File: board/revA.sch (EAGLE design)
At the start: 37 parts, among them IC1 74HCT125D, Q1 VND7NV04, Q2 VND7NV04, Q3 VND7NV04, Q4 VND7NV04

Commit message: Changing buffer package to TSSOP
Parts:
- IC1: value 74HCT125D -> 74HCT125; device 74xx-eu:74HCT125D -> 74xx-eu:74ABT125PW
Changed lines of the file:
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@@
 <grid distance="0.05" unitdist="inch" unit="inch" style="lines" multiple="1" display="yes" altdistance="0.005" altunitdist="inch" altunit="inch"/>
 <layers>
-<layer number="1" name="Top" color="4" fill="1" visible="no" active="no"/>
-<layer number="16" name="Bottom" color="1" fill="1" visible="no" active="no"/>
-<layer number="17" name="Pads" color="2" fill="1" visible="no" active="no"/>
-<layer number="18" name="Vias" color="2" fill="1" visible="no" active="no"/>
-<layer number="19" name="Unrouted" color="6" fill="1" visible="no" active="no"/>
-<layer number="20" name="Dimension" color="24" fill="1" visible="no" active="no"/>
-<layer number="21" name="tPlace" color="7" fill="1" visible="no" active="no"/>
-<layer number="22" name="bPlace" color="7" fill="1" visible="no" active="no"/>
-<layer number="23" name="tOrigins" color="15" fill="1" visible="no" active="no"/>
-<layer number="24" name="bOrigins" color="15" fill="1" visible="no" active="no"/>
-<layer number="25" name="tNames" color="7" fill="1" visible="no" active="no"/>
-<layer number="26" name="bNames" color="7" fill="1" visible="no" active="no"/>
-<layer number="27" name="tValues" color="7" fill="1" visible="no" active="no"/>
-<layer number="28" name="bValues" color="7" fill="1" visible="no" active="no"/>
+<layer number="1" name="Top" color="4" fill="1" visible="yes" active="no"/>
+<layer number="16" name="Bottom" color="1" fill="1" visible="yes" active="no"/>
+<layer number="17" name="Pads" color="2" fill="1" visible="yes" active="no"/>
+<layer number="18" name="Vias" color="2" fill="1" visible="yes" active="no"/>
+<layer number="19" name="Unrouted" color="6" fill="1" visible="yes" active="no"/>
+<layer number="20" name="Dimension" color="24" fill="1" visible="yes" active="no"/>
+<layer number="21" name="tPlace" color="7" fill="1" visible="yes" active="no"/>
+<layer number="22" name="bPlace" color="7" fill="1" visible="yes" active="no"/>
+<layer number="23" name="tOrigins" color="15" fill="1" visible="yes" active="no"/>
+<layer number="24" name="bOrigins" color="15" fill="1" visible="yes" active="no"/>
+<layer number="25" name="tNames" color="7" fill="1" visible="yes" active="no"/>
+<layer number="26" name="bNames" color="7" fill="1" visible="yes" active="no"/>
+<layer number="27" name="tValues" color="7" fill="1" visible="yes" active="no"/>
+<layer number="28" name="bValues" color="7" fill="1" visible="yes" active="no"/>
 <layer number="29" name="tStop" color="7" fill="3" visible="no" active="no"/>
 <layer number="30" name="bStop" color="7" fill="6" visible="no" active="no"/>
@@
 <layer number="35" name="tGlue" color="7" fill="4" visible="no" active="no"/>
 <layer number="36" name="bGlue" color="7" fill="5" visible="no" active="no"/>
-<layer number="37" name="tTest" color="7" fill="1" visible="no" active="no"/>
-<layer number="38" name="bTest" color="7" fill="1" visible="no" active="no"/>
+<layer number="37" name="tTest" color="7" fill="1" visible="yes" active="no"/>
+<layer number="38" name="bTest" color="7" fill="1" visible="yes" active="no"/>
 <layer number="39" name="tKeepout" color="4" fill="11" visible="no" active="no"/>
 <layer number="40" name="bKeepout" color="1" fill="11" visible="no" active="no"/>
@@
 <layer number="44" name="Drills" color="7" fill="1" visible="no" active="no"/>
 <layer number="45" name="Holes" color="7" fill="1" visible="no" active="no"/>
-<layer number="46" name="Milling" color="3" fill="1" visible="no" active="no"/>
-<layer number="47" name="Measures" color="7" fill="1" visible="no" active="no"/>
-<layer number="48" name="Document" color="7" fill="1" visible="no" active="no"/>
-<layer number="49" name="Reference" color="7" fill="1" visible="no" active="no"/>
-<layer number="50" name="dxf" color="7" fill="1" visible="no" active="no"/>
-<layer number="51" name="tDocu" color="7" fill="1" visible="no" active="no"/>
-<layer number="52" name="bDocu" color="7" fill="1" visible="no" active="no"/>
-<layer number="53" name="tGND_GNDA" color="7" fill="9" visible="no" active="no"/>
-<layer number="54" name="bGND_GNDA" color="1" fill="9" visible="no" active="no"/>
-<layer number="56" name="wert" color="7" fill="1" visible="no" active="no"/>
-<layer number="57" name="tCAD" color="7" fill="1" visible="no" active="no"/>
-<layer number="59" name="tCarbon" color="7" fill="1" visible="no" active="no"/>
-<layer number="60" name="bCarbon" color="7" fill="1" visible="no" active="no"/>
+<layer number="46" name="Milling" color="3" fill="1" visible="yes" active="no"/>
+<layer number="47" name="Measures" color="7" fill="1" visible="yes" active="no"/>
+<layer number="48" name="Document" color="7" fill="1" visible="yes" active="no"/>
+<layer number="49" name="Reference" color="7" fill="1" visible="yes" active="no"/>
+<layer number="50" name="dxf" color="7" fill="1" visible="yes" active="no"/>
+<layer number="51" name="tDocu" color="7" fill="1" visible="yes" active="no"/>
+<layer number="52" name="bDocu" color="7" fill="1" visible="yes" active="no"/>
+<layer number="53" name="tGND_GNDA" color="7" fill="9" visible="yes" active="no"/>
+<layer number="54" name="bGND_GNDA" color="1" fill="9" visible="yes" active="no"/>
+<layer number="56" name="wert" color="7" fill="1" visible="yes" active="no"/>
+<layer number="57" name="tCAD" color="7" fill="1" visible="yes" active="no"/>
+<layer number="59" name="tCarbon" color="7" fill="1" visible="yes" active="no"/>
+<layer number="60" name="bCarbon" color="7" fill="1" visible="yes" active="no"/>
 <layer number="88" name="SimResults" color="9" fill="1" visible="yes" active="yes"/>
 <layer number="89" name="SimProbes" color="9" fill="1" visible="yes" active="yes"/>
@@
 <part name="UART" library="SparkFun-Connectors" library_urn="urn:adsk.eagle:library:513" deviceset="CONN_03" device="" package3d_urn="urn:adsk.eagle:package:38063/1"/>
 <part name="GND13" library="supply1" library_urn="urn:adsk.eagle:library:371" deviceset="GND" device=""/>
-<part name="IC1" library="74xx-eu" library_urn="urn:adsk.eagle:library:85" deviceset="74*125" device="D" package3d_urn="urn:adsk.eagle:package:1010/2" technology="HCT"/>
+<part name="IC1" library="74xx-eu" library_urn="urn:adsk.eagle:library:85" deviceset="74*125" device="PW" package3d_urn="urn:adsk.eagle:package:2019/1" technology="ABT" value="74HCT125"/>
 <part name="P+2" library="supply1" library_urn="urn:adsk.eagle:library:371" deviceset="+5V" device=""/>
 <part name="GND14" library="supply1" library_urn="urn:adsk.eagle:library:371" deviceset="GND" device=""/>

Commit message: Adding wires, protections, switch
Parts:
- added D10, D11, D8, D9: BAT54S, diode:BAT54S
- added K1: (no value), Seeed-Switch:SMD-SWITCH-TACTILE-SPST-NO(4P-D6.0MM)
- added R12, R13, R14, R15, R16: 10k, rcl:R-EU_R0603
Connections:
- removed net INJ1_FAKE: INJ.1, R7.1
- removed net INJ2_FAKE: INJ.2, R8.1
- removed net INJ3_FAKE: INJ.3, R9.1
- removed net INJ4_FAKE: INJ.4, R10.1
- new net BUTTON1: MCUPORTC.PC13
- new net INJ1_FREQ: D8.C1A2, MCUPORTA_L.PA6, R12.1
- new net INJ1_IN: INJ.1, R12.2, R7.1
- new net INJ2_FREQ: D9.C1A2, MCUPORTA_L.PA7, R13.1
- new net INJ2_IN: INJ.2, R13.2, R8.1
- new net INJ3_FREQ: D10.C1A2, MCUPORTB_L.PB0, R14.1
- new net INJ3_IN: INJ.3, R14.2, R9.1
- new net INJ4_FREQ: D11.C1A2, MCUPORTB_L.PB1, R15.1
- new net INJ4_IN: INJ.4, R10.1, R15.2
- new net N$3: K1.A0, K1.A1, MCURESET.BOOT0, R16.1
- new net SPI_MISO: MCUPORTB_H.PB14
- new net SPI_MOSI: MCUPORTB_H.PB15
- new net SPI_NSS: MCUPORTB_H.PB12
- new net SPI_SCK: MCUPORTB_H.PB13
- net +3V3: now also D10.C2, D11.C2, D8.C2, D9.C2, K1.B0, K1.B1; no longer MCURESET.BOOT0
- net AN_0: now also MCUPORTA_L.PA0
- net AN_1: now also MCUPORTA_L.PA4
- net GND: now also D10.A1, D11.A1, D8.A1, D9.A1, R16.2
- net INJ1_TRIGGER: now also IC1A.I; no longer IC1B.I
- net INJ2_TRIGGER: now also IC1B.I; no longer IC1A.I
- net N$7: now also IC1A.O; no longer IC1B.O
- net N$8: now also IC1B.O; no longer IC1A.O
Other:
- moved on the sheet: IC1A, IC1B

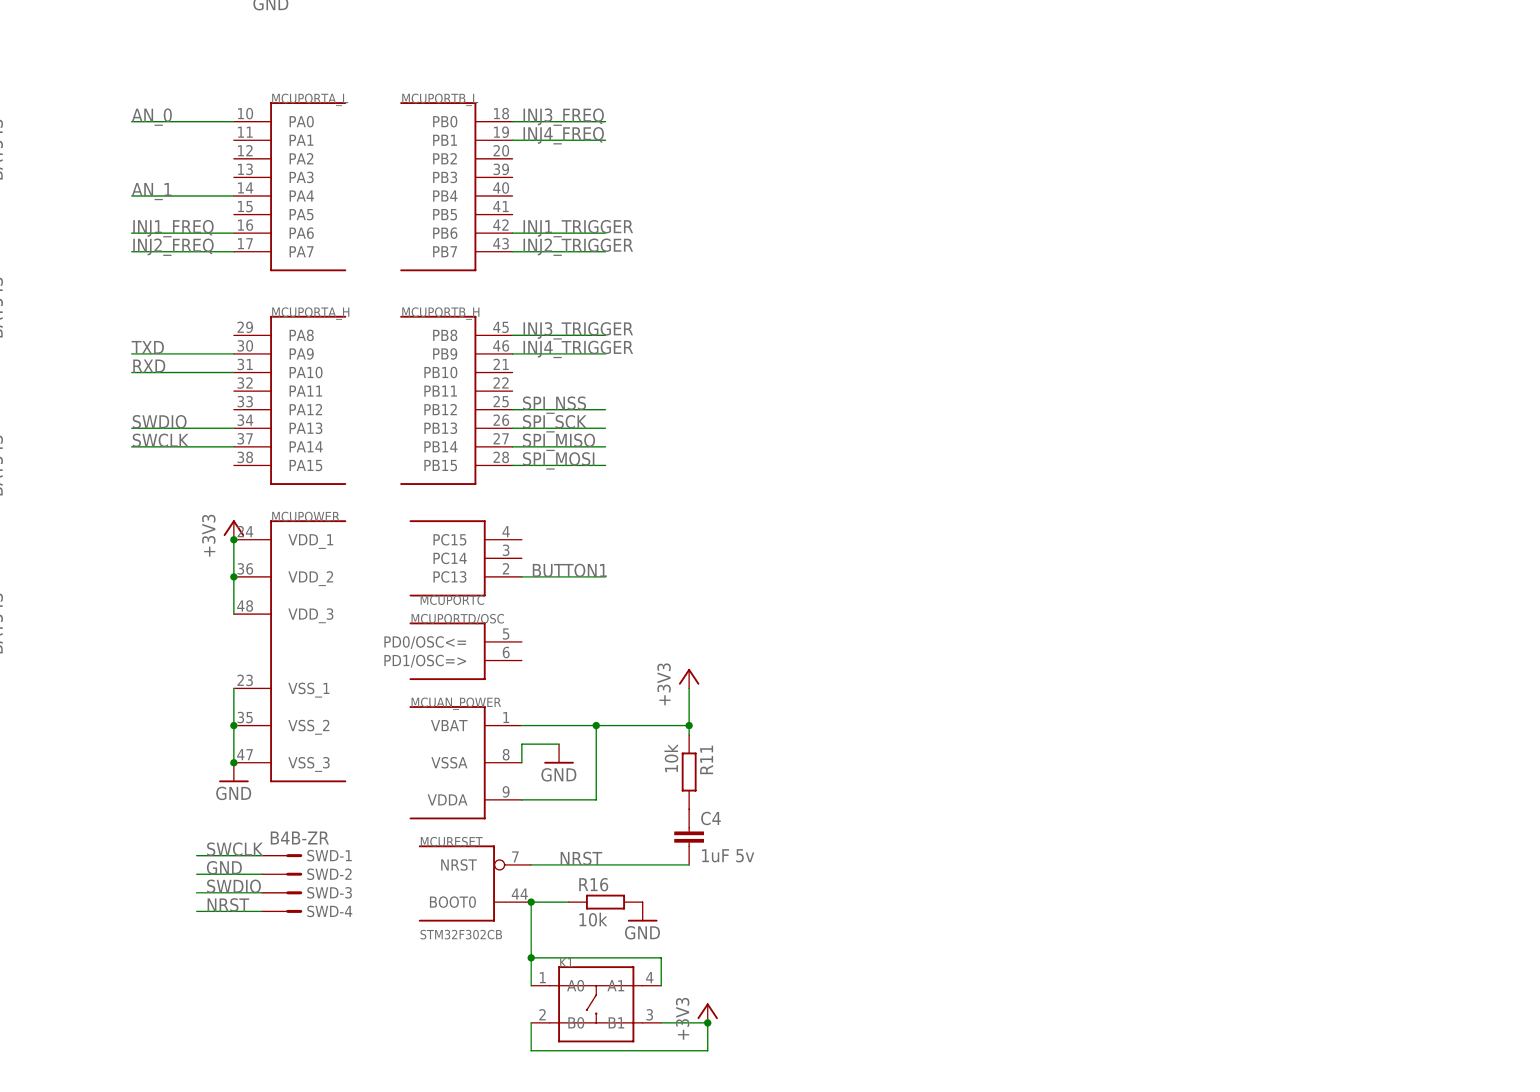
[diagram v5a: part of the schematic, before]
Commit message: More routing, adding interfaces
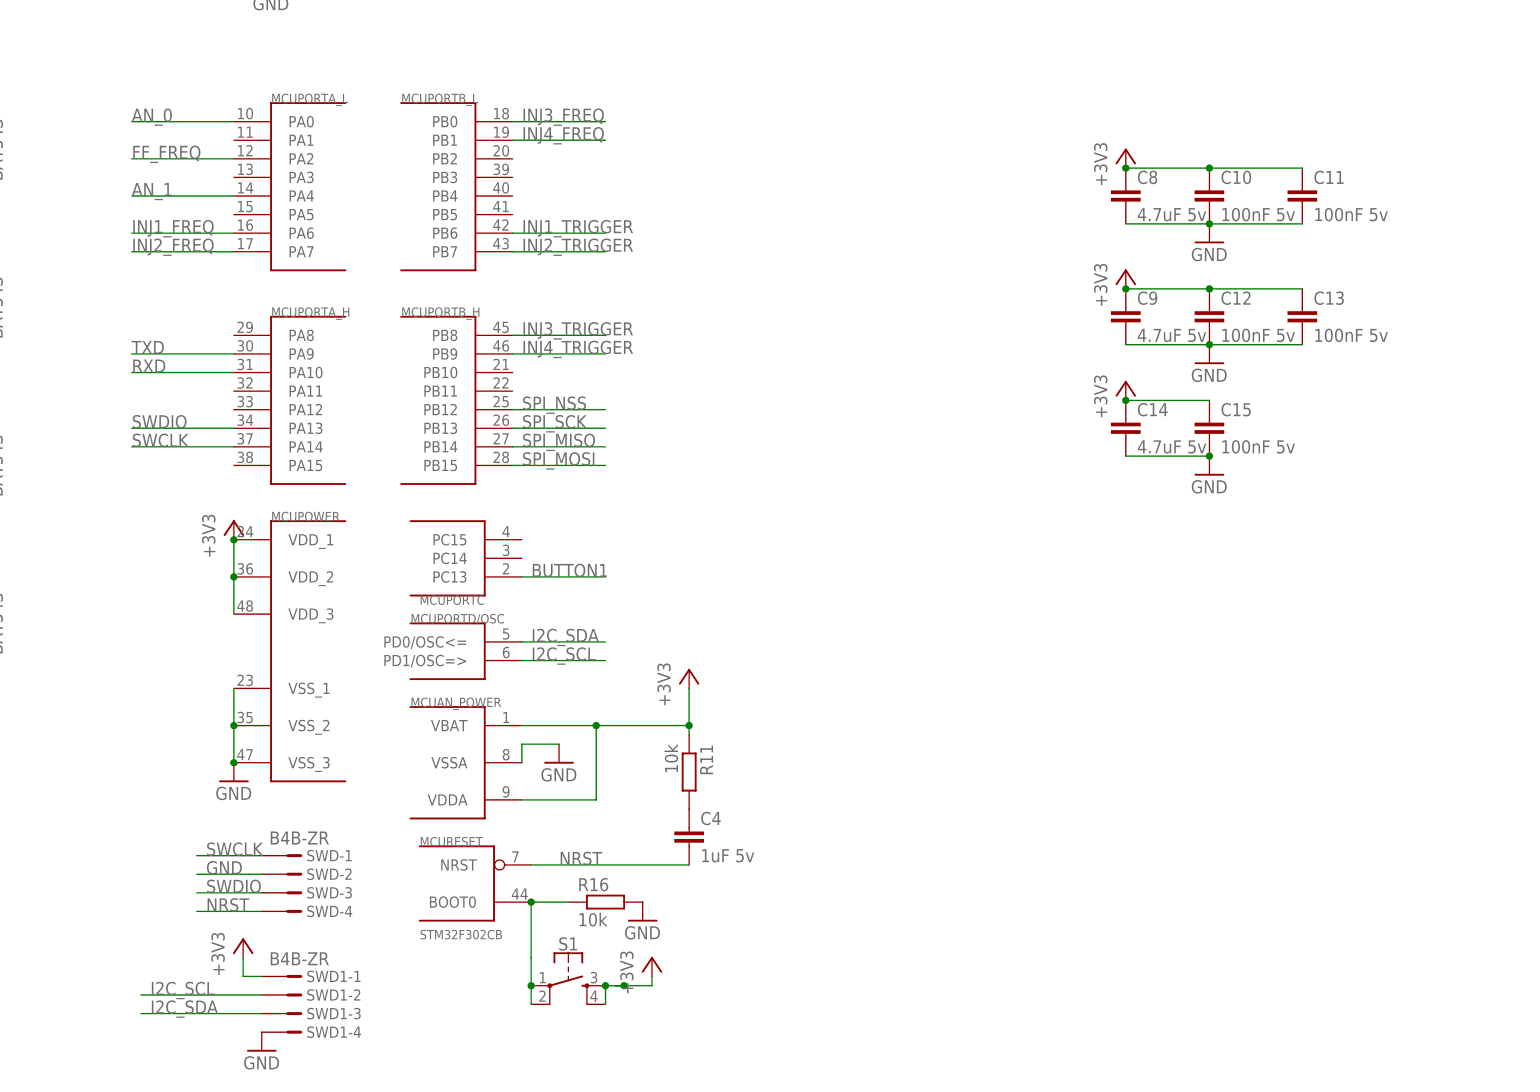
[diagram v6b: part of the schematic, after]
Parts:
- removed K1: (no value), Seeed-Switch:SMD-SWITCH-TACTILE-SPST-NO(4P-D6.0MM)
- added C10, C11, C12, C13, C15: 100nF 5v, rcl:C-EUC0603
- added C14, C8, C9: 4.7uF 5v, rcl:C-EUC0603
- added S1: (no value), SparkFun-Switches:MOMENTARY-SWITCH-SPST-2-SMD-5.2MM
- added SWD1: B4B-ZR, con-jst:B4B-ZR
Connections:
- removed net N$3: K1.A0, K1.A1, MCURESET.BOOT0, R16.1
- new net I2C_SCL: MCUPORTD/OSC.PD1/OSC=>, SWD1-2.1
- new net I2C_SDA: MCUPORTD/OSC.PD0/OSC<=, SWD1-3.1
- new net N$5: MCURESET.BOOT0, R16.1, S1.1, S1.2
- net +3V3: now also C10.1, C11.1, C12.1, C13.1, C14.1, C15.1, C8.1, C9.1, S1.3, S1.4, SWD1-1.1; no longer K1.B0, K1.B1
- net FF_FREQ: now also MCUPORTA_L.PA2
- net GND: now also C10.2, C11.2, C12.2, C13.2, C14.2, C15.2, C8.2, C9.2, SWD1-4.1

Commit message: Testing autorouter
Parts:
- renumbered SWD1 to I2C
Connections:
- net INJ1: now also Q3.S; no longer Q2.S
- net INJ1_TRIGGER: now also IC1C.I; no longer IC1A.I
- net INJ2: now also Q4.S; no longer Q1.S
- net INJ2_TRIGGER: now also IC1D.I; no longer IC1B.I
- net INJ3: now also Q1.S; no longer Q4.S
- net INJ3_TRIGGER: now also IC1B.I; no longer IC1D.I
- net INJ4: now also Q2.S; no longer Q3.S
- net INJ4_TRIGGER: now also IC1A.I; no longer IC1C.I

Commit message: More routing tests
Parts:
- removed INJ: (no value), SparkFun-Connectors:CONN_04
- removed J1: (no value), SparkFun-Connectors:CONN_10"
- added ANALOG, SENSOR: (no value), SparkFun-Connectors:CONN_03POLAR_LOCK
- added INJ_IN, INJ_OUT: (no value), SparkFun-Connectors:CONN_04POLAR_LOCK
- I2C: value B4B-ZR -> (none); device con-jst:B4B-ZR -> SparkFun-Connectors:CONN_04POLAR_LOCK
- R10, R7, R8, R9: device rcl:R-EU_0207/7 -> rcl:R-EU_0414/15
- UART: device SparkFun-Connectors:CONN_03 -> SparkFun-Connectors:CONN_03POLAR_LOCK
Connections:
- net N$5 renamed BUTTON
- net +3V3: now also I2C.1; no longer I2C-1.1
- net AN1: now also ANALOG.2; no longer J1.6
- net FF_SIG: now also SENSOR.2; no longer J1.8
- net GND: now also ANALOG.1, I2C.4, SENSOR.1; no longer I2C-4.1, J1.1, J1.7
- net I2C_SCL: now also I2C.3; no longer I2C-2.1
- net I2C_SDA: now also I2C.2; no longer I2C-3.1
- net INJ1: now also INJ_OUT.1, Q1.S; no longer J1.2, Q3.S
- net INJ1_IN: now also INJ_IN.1; no longer INJ.1
- net INJ2: now also INJ_OUT.2, Q2.S; no longer J1.3, Q4.S
- net INJ2_IN: now also INJ_IN.2; no longer INJ.2
- net INJ3: now also INJ_OUT.3, Q3.S; no longer J1.4, Q1.S
- net INJ3_IN: now also INJ_IN.3; no longer INJ.3
- net INJ3_TRIGGER: now also IC1A.I; no longer IC1B.I
- net INJ4: now also INJ_OUT.4, Q4.S; no longer J1.5, Q2.S
- net INJ4_IN: now also INJ_IN.4; no longer INJ.4
- net INJ4_TRIGGER: now also IC1B.I; no longer IC1A.I
- net N$10: now also IC1A.O; no longer IC1C.O
- net N$7: now also IC1D.O; no longer IC1A.O
- net N$8: now also IC1C.O; no longer IC1B.O
- net N$9: now also IC1B.O; no longer IC1D.O
- net SWCLK: now also SWD-3.1; no longer SWD-1.1
- net SWDIO: now also SWD-1.1; no longer SWD-3.1
- net VCC: now also ANALOG.3, SENSOR.3; no longer J1.10, J1.9
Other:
- moved on the sheet: IC1A, IC1B, IC1C, IC1D, R6
